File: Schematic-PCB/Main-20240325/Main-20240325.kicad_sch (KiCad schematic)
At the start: 36 parts, among them J1 Conn_01x20_Pin, J2 Conn_01x03_Pin, J3 Conn_01x10_Pin, J4 Conn_01x03_Pin, J5 Conn_01x15_Pin, J6 Conn_02x05_Odd_Even, J7 Conn_02x05_Odd_Even, U2 DEV-16771, U3 MOUDLE-SEEEDUINO-XIAO-ESP32C3

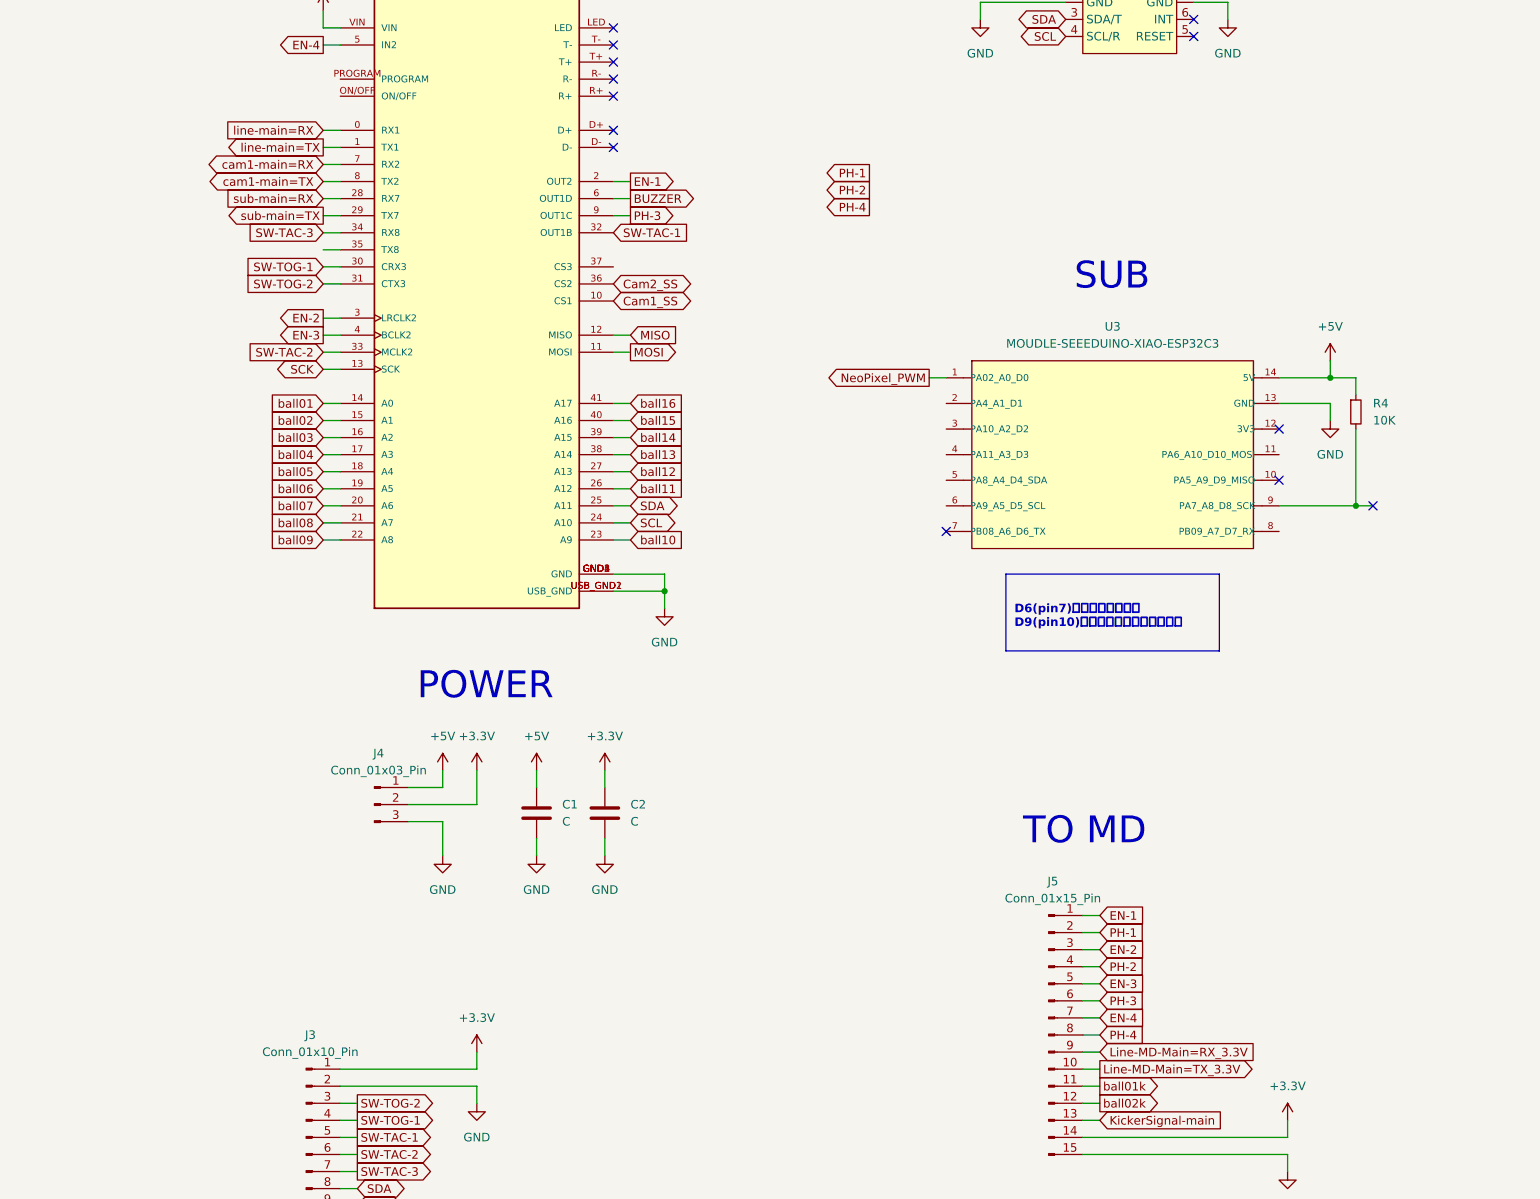
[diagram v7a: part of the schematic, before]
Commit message: メイン基板の回路図を修正しました
・RX・TXの逆転の修正
・ESP32C3のpin9への印加電圧を5V→3.3Vへ修正
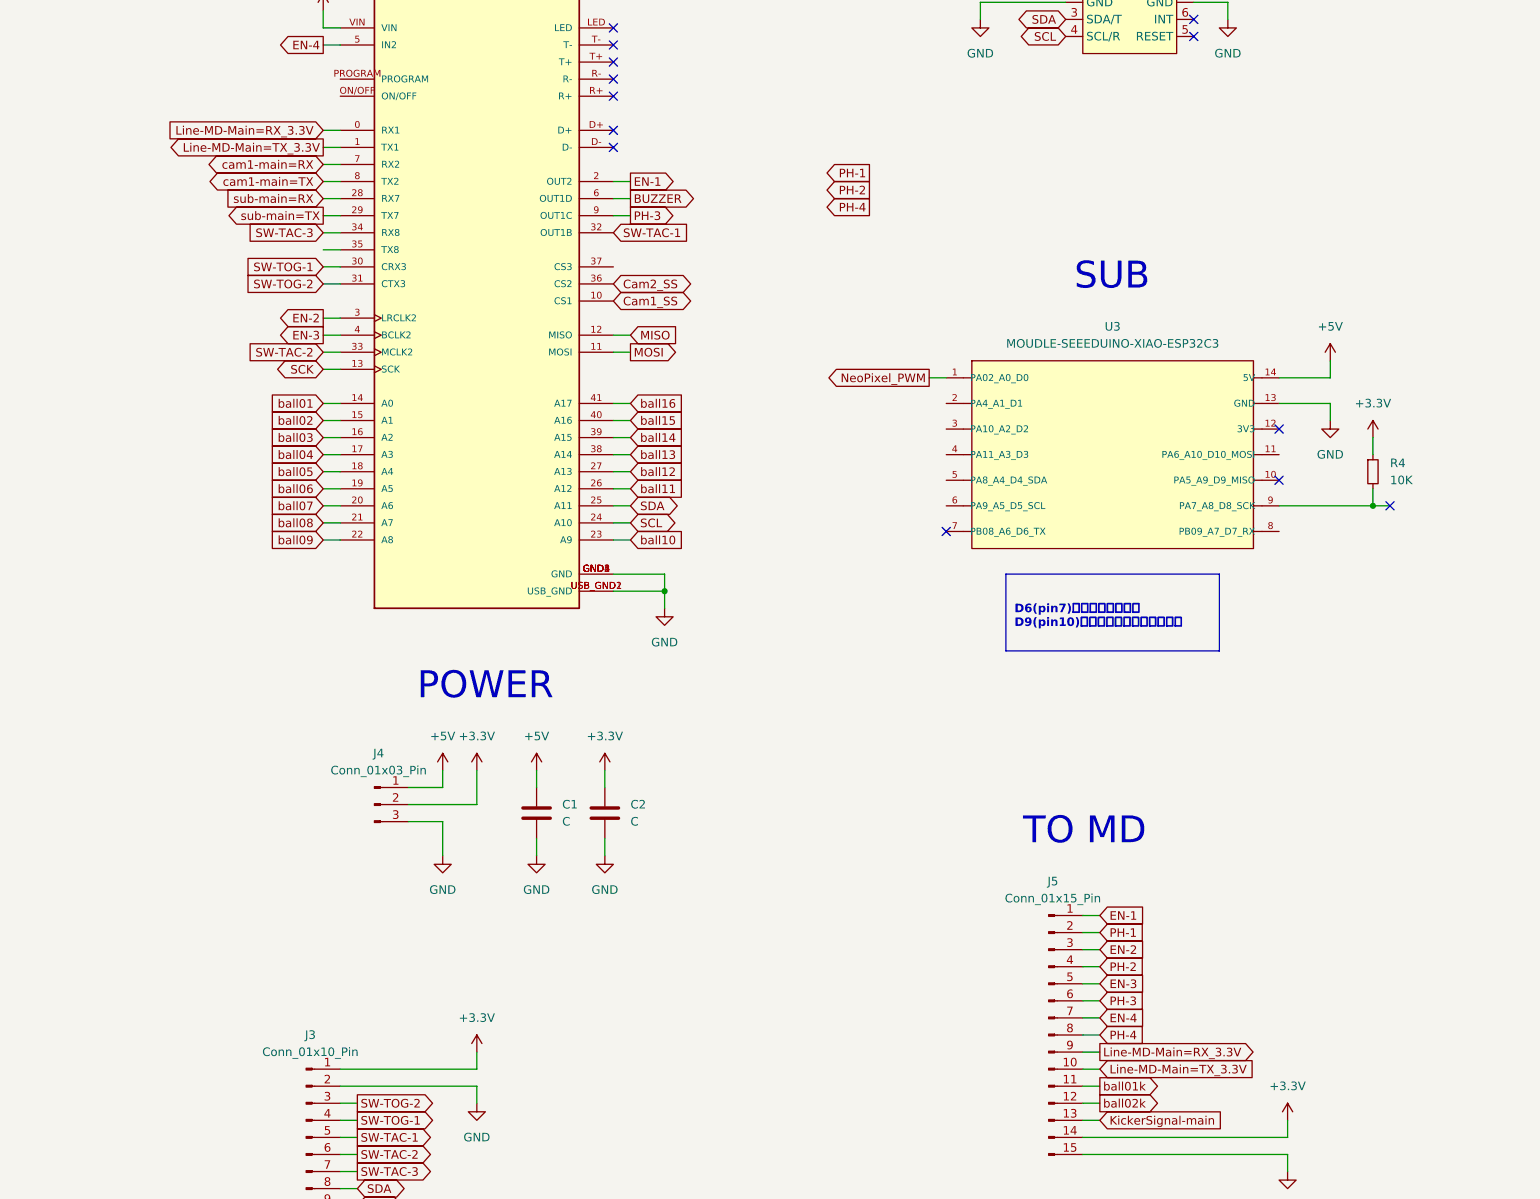
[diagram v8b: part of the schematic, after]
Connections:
- net line-main=RX is gone; now on net Line-MD-Main=RX_3.3V: U2.0 (RX1)
- net line-main=TX is gone; now on net Line-MD-Main=TX_3.3V: U2.1 (TX1)
- net +3.3V: now also R4.1
- net +5V: no longer R4.1
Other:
- moved on the sheet: R4
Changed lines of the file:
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@@
 	)
 	(junction
-		(at 208.28 119.38)
-		(diameter 0)
-		(color 0 0 0 0)
-	)
-	(junction
 		(at 274.32 138.43)
 		(diameter 0)
@@
 	)
 	(junction
-		(at -81.28 52.07)
+		(at 210.82 119.38)
 		(diameter 0)
 		(color 0 0 0 0)
 	)
 	(junction
-		(at 204.47 100.33)
+		(at -81.28 52.07)
 		(diameter 0)
 		(color 0 0 0 0)
 	)
 	(no_connect
-		(at 210.82 119.38)
+		(at 213.36 119.38)
 	)
 	(no_connect
@@
 	(wire
 		(pts
-			(xy 208.28 100.33) (xy 208.28 102.87)
+			(xy 210.82 109.22) (xy 210.82 111.76)
 		)
 		(stroke
@@
 	(wire
 		(pts
-			(xy 208.28 107.95) (xy 208.28 119.38)
+			(xy 210.82 116.84) (xy 210.82 119.38)
 		)
 		(stroke
@@
 	(wire
 		(pts
-			(xy 208.28 119.38) (xy 210.82 119.38)
-		)
-		(stroke
-			(width 0)
-			(type default)
-		)
-	)
-	(wire
-		(pts
 			(xy -24.13 163.83) (xy -26.67 163.83)
 		)
@@
 	(wire
 		(pts
-			(xy 204.47 100.33) (xy 208.28 100.33)
+			(xy -81.28 54.61) (xy -81.28 52.07)
 		)
 		(stroke
@@
 	(wire
 		(pts
-			(xy -81.28 54.61) (xy -81.28 52.07)
+			(xy 72.39 171.45) (xy 72.39 166.37)
 		)
 		(stroke
@@
 	(wire
 		(pts
-			(xy 72.39 171.45) (xy 72.39 166.37)
+			(xy 54.61 91.44) (xy 57.15 91.44)
 		)
 		(stroke
@@
 	(wire
 		(pts
-			(xy 54.61 91.44) (xy 57.15 91.44)
+			(xy 54.61 78.74) (xy 57.15 78.74)
 		)
 		(stroke
@@
 	(wire
 		(pts
-			(xy 54.61 78.74) (xy 57.15 78.74)
+			(xy -10.16 76.2) (xy -26.67 76.2)
 		)
 		(stroke
@@
 	(wire
 		(pts
-			(xy -10.16 76.2) (xy -26.67 76.2)
+			(xy 77.47 158.75) (xy 77.47 163.83)
 		)
 		(stroke
@@
 	(wire
 		(pts
-			(xy 77.47 158.75) (xy 77.47 163.83)
+			(xy 210.82 119.38) (xy 213.36 119.38)
 		)
 		(stroke
@@
 	(wire
 		(pts
-			(xy 196.85 119.38) (xy 208.28 119.38)
+			(xy 196.85 119.38) (xy 210.82 119.38)
 		)
 		(stroke
@@
 		)
 	)
-	(global_label "line-main=RX"
+	(global_label "Line-MD-Main=RX_3.3V"
 		(shape input)
 		(at 54.61 63.5 180)
@@
 		)
 		(property "Intersheetrefs" "${INTERSHEET_REFS}"
-			(at 37.8968 63.5 0)
+			(at 28.402 63.5 0)
 			(effects
 				(font
@@
 	)
 	(global_label "Line-MD-Main=TX_3.3V"
-		(shape output)
+		(shape input)
 		(at 170.18 203.2 0)
 		(fields_autoplaced yes)
@@
 	)
 	(global_label "Line-MD-Main=RX_3.3V"
-		(shape input)
+		(shape output)
 		(at 170.18 200.66 0)
 		(fields_autoplaced yes)
@@
 		)
 	)
-	(global_label "line-main=TX"
+	(global_label "Line-MD-Main=TX_3.3V"
 		(shape output)
 		(at 54.61 66.04 180)
@@
 		)
 		(property "Intersheetrefs" "${INTERSHEET_REFS}"
-			(at 38.1992 66.04 0)
+			(at 28.7044 66.04 0)
 			(effects
 				(font
@@
 	(symbol
 		(lib_id "Device:R_Small")
-		(at 208.28 105.41 0)
+		(at 210.82 114.3 0)
 		(unit 1)
 		(exclude_from_sim no)
@@
 		(fields_autoplaced yes)
 		(property "Reference" "R4"
-			(at 210.82 104.14 0)
+			(at 213.36 113.03 0)
 			(effects
 				(font
@@
 		)
 		(property "Value" "10K"
-			(at 210.82 106.68 0)
+			(at 213.36 115.57 0)
 			(effects
 				(font
@@
 		)
 		(property "Footprint" ""
-			(at 208.28 105.41 0)
+			(at 210.82 114.3 0)
 			(effects
 				(font
@@
 		)
 		(property "Datasheet" "~"
-			(at 208.28 105.41 0)
+			(at 210.82 114.3 0)
 			(effects
 				(font
@@
 		)
 		(property "Description" "Resistor, small symbol"
-			(at 208.28 105.41 0)
+			(at 210.82 114.3 0)
 			(effects
 				(font
@@
 					(unit 1)
 				)
+			)
+		)
+	)
+	(symbol
+		(lib_id "power:+3.3V")
+		(at 210.82 109.22 0)
+		(unit 1)
+		(exclude_from_sim no)
+		(in_bom yes)
+		(on_board yes)
+		(dnp no)
+		(fields_autoplaced yes)
+		(property "Reference" "#PWR030"
+			(at 210.82 113.03 0)
+			(effects
+				(font
+					(size 1.27 1.27)
+				)
+				(hide yes)
+			)
+		)
+		(property "Value" "+3.3V"
+			(at 210.82 104.14 0)
+			(effects
+				(font
+					(size 1.27 1.27)
+				)
+			)
+		)
+		(property "Footprint" ""
+			(at 210.82 109.22 0)
+			(effects
+				(font
+					(size 1.27 1.27)
+				)
+				(hide yes)
+			)
+		)
+		(property "Datasheet" ""
+			(at 210.82 109.22 0)
+			(effects
+				(font
+					(size 1.27 1.27)
+				)
+				(hide yes)
+			)
+		)
+		(property "Description" "Power symbol creates a global label with name \"+3.3V\""
+			(at 210.82 109.22 0)
+			(effects
+				(font
+					(size 1.27 1.27)
+				)
+				(hide yes)
+			)
+		)
+		(pin "1"
+		)
+		(instances
+			(project "Main-20240325"
+				(path "/d42c2da0-c5d1-4e9e-abe5-6ac5f9ded35c"
+					(reference "#PWR030")
+					(unit 1)
+				)
